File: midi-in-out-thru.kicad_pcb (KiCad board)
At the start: 2 copper layers, 72.6 x 48 mm, 19 parts, among them J1 uC, J2 IN, J3 OUT, J4 THRU, U1 74HC14, U2 H11L1

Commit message: Completed initial layout
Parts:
- added C3: 100n, Capacitor_THT:C_Disc_D3.8mm_W2.6mm_P2.50mm, F.Cu at (93.7, 52.1)
- added H1: MountingHole, MountingHole:MountingHole_3.2mm_M3, F.Cu at (86.0, 34.0)
- added H2: MountingHole, MountingHole:MountingHole_3.2mm_M3, F.Cu at (154.0, 34.0)
- added H3: MountingHole, MountingHole:MountingHole_3.2mm_M3, F.Cu at (86.0, 66.0)
- added H4: MountingHole, MountingHole:MountingHole_3.2mm_M3, F.Cu at (154.0, 66.0)
- J2, J3, J4: footprint eurocad:MIDI_DIN5 -> Personal:MIDI_DIN5
- moved J1 27.5 mm to (150.0, 52.8), turned to 0 degrees
- moved D1 16.3 mm to (87.6, 59.2), turned to 90 degrees
- moved C1 11.4 mm to (107.4, 52.1), turned to 0 degrees
- moved R8 10.9 mm to (140.2, 52.1), turned to 180 degrees
- moved R1 10.7 mm to (140.2, 63.0), turned to 180 degrees
- moved R3 9.88 mm to (103.9, 53.3), turned to -90 degrees
- moved R6 8.87 mm to (123.7, 52.1), turned to 180 degrees
- moved U1 6.48 mm to (108.0, 63.0)
- moved U2 6.23 mm to (94.7, 63.0)
- moved R7 5.95 mm to (127.3, 63.0), turned to 90 degrees
- moved R5 5.43 mm to (90.7, 61.7)
- moved R2 5.11 mm to (140.2, 55.6)
- moved LED1 3.74 mm to (143.8, 59.3), turned to -90 degrees
- moved LED2 3.21 mm to (143.8, 52.6)
- moved C2 2.05 mm to (98.6, 52.1)
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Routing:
- net /RX: track 0.00 -> 62.7 mm
- net /TX: track 0.00 -> 48.2 mm
- net Net-(D1-Pad2): track 0.00 -> 36.7 mm
- net Net-(J4-Pad5): track 0.00 -> 21.2 mm
- net Net-(R1-Pad2): track 0.00 -> 21.1 mm
- net Net-(R2-Pad2): track 0.00 -> 18.6 mm
- net Net-(C2-Pad1): track 0.00 -> 10.3 mm
- net Net-(J4-Pad4): track 0.00 -> 9.25 mm
- net Net-(J3-Pad5): track 0.00 -> 8.90 mm
- net Net-(D1-Pad1): track 0.00 -> 8.69 mm
- net Net-(R9-Pad1): track 0.00 -> 8.49 mm
- net Net-(J2-Pad4): track 0.00 -> 8.48 mm
- net Net-(J3-Pad4): track 0.00 -> 7.81 mm
- net Net-(R7-Pad1): track 0.00 -> 7.75 mm
- net Net-(LED1-Pad2): track 0.00 -> 4.08 mm
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- added copper zone on F.Cu, net +3.3V
- added copper zone on B.Cu, net GND
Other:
- board size 72.6 x 48 mm -> 76 x 40 mm
- copper layers 2 -> 4
- board text added: "GND"
- board text added: "IN"
- board text added: "MIDI In/Out/Thru Rev. 1"
- board text added: "OUT"
- board text added: "Paul Battley po-ru.com"
- board text added: "RX"
- board text added: "THRU"
- board text added: "TX"
- board text added: "VCC"
- board text added: "☐ 3.3V ☐ 5V"

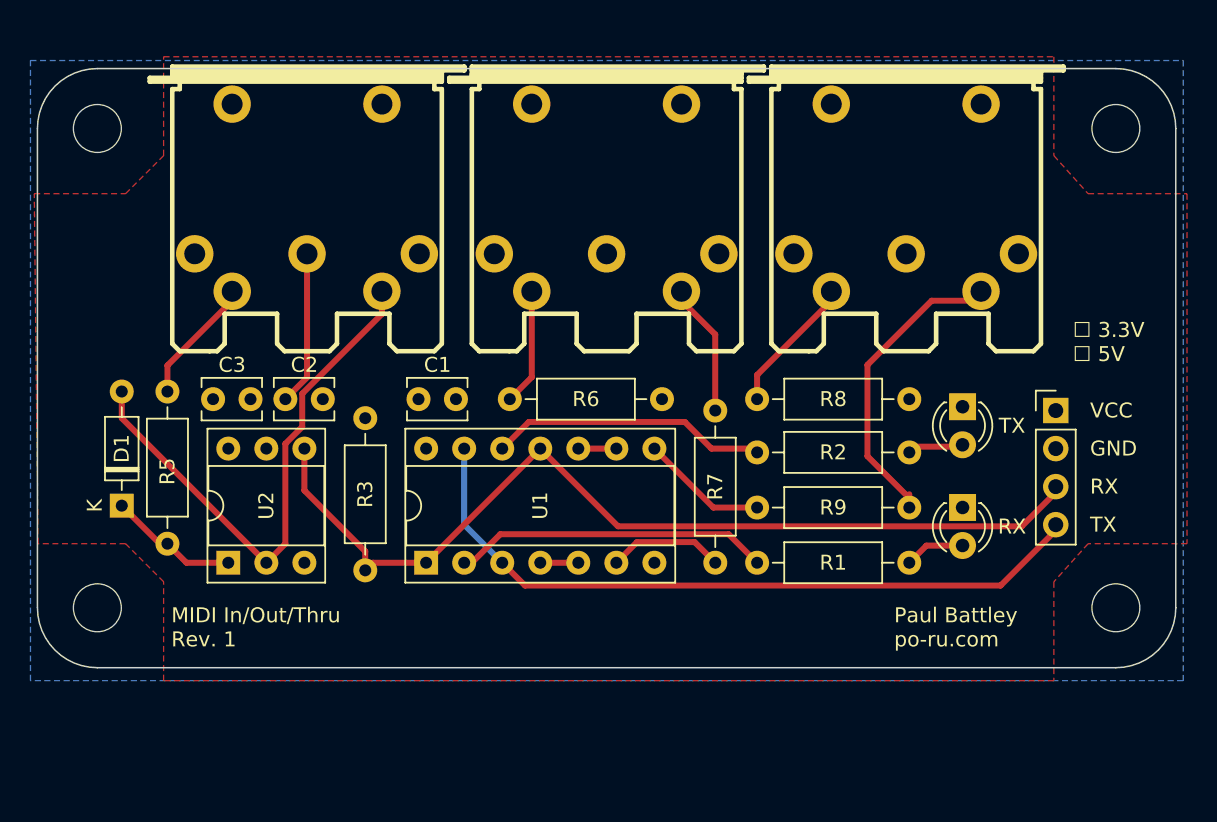
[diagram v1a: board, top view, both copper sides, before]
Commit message: Smaller resistors, neater layout
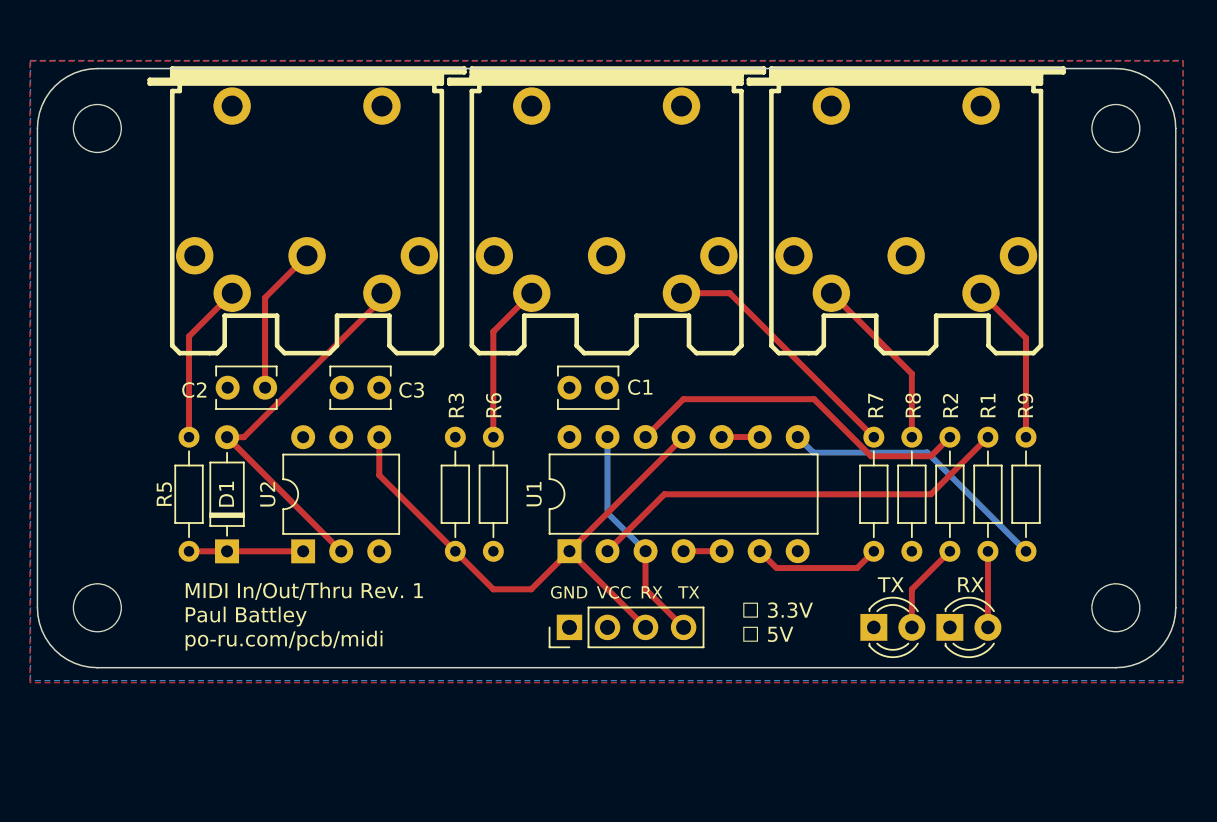
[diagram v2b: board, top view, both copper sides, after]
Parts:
- H1, H2, H3, H4: footprint MountingHole:MountingHole_3.2mm_M3 -> Personal:MountingHole_3.2mm_M3
- R1, R2, R3, R5, R6, R7, R8, R9: footprint Resistor_THT:R_Axial_DIN0207_L6.3mm_D2.5mm_P10.16mm_Horizontal -> Resistor_THT:R_Axial_DIN0204_L3.6mm_D1.6mm_P7.62mm_Horizontal
- U1: footprint Package_DIP:DIP-14_W7.62mm_Socket -> Package_DIP:DIP-14_W7.62mm
- U2: footprint Package_DIP:DIP-6_W7.62mm_Socket -> Package_DIP:DIP-6_W7.62mm
- moved J1 35.5 mm to (117.5, 67.3), turned to 90 degrees
- moved R9 18.2 mm to (148.0, 62.2), turned to 90 degrees
- moved LED2 15.9 mm to (137.8, 67.3), turned to 0 degrees
- moved R6 15.2 mm to (112.4, 62.2), turned to 90 degrees
- moved C3 11.1 mm to (104.8, 51.3), turned to 180 degrees
- moved R7 10.6 mm to (137.8, 62.2)
- moved R8 10.2 mm to (140.4, 62.2), turned to 90 degrees
- moved C1 10.1 mm to (117.5, 51.3)
- moved U1 9.60 mm to (117.5, 62.2)
- moved LED1 8.05 mm to (142.9, 67.3), turned to 0 degrees
- moved D1 7.66 mm to (94.7, 62.2)
- moved R2 7.14 mm to (142.9, 62.2), turned to 90 degrees
- moved R3 6.15 mm to (109.9, 54.6)
- moved R1 5.31 mm to (145.5, 62.2), turned to 90 degrees
- moved U2 5.06 mm to (99.7, 62.2)
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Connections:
- C3 pad 1: +3.3V -> GND
- J1 pad 1: +3.3V -> GND
- J1 pad 2: GND -> +3.3V
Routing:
- net /TX: track 48.2 -> 14.8 mm
- net /RX: track 62.7 -> 37.4 mm
- net Net-(D1-Pad2): track 36.7 -> 25.3 mm
- net Net-(J4-Pad5): track 21.2 -> 10.9 mm
- net Net-(R9-Pad1): track 8.49 -> 18.4 mm
- net Net-(J3-Pad5): track 8.90 -> 16.8 mm
- net Net-(R1-Pad2): track 21.1 -> 28.6 mm
- net Net-(R2-Pad2): track 18.6 -> 23.5 mm
- net Net-(J3-Pad4): track 7.81 -> 10.7 mm
- net Net-(J4-Pad4): track 9.25 -> 11.8 mm
- net Net-(LED2-Pad2): track 3.77 -> 6.13 mm
- net Net-(J2-Pad4): track 8.48 -> 10.8 mm
- net Net-(D1-Pad1): track 8.69 -> 7.62 mm
- net Net-(LED1-Pad2): track 4.08 -> 5.08 mm
- net Net-(R7-Pad1): track 7.75 -> 8.55 mm
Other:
- board text added: "MIDI In/Out/Thru Rev. 1 Paul Battley po-ru.com/pcb/midi"
- board text removed: "MIDI In/Out/Thru Rev. 1"
- board text removed: "Paul Battley po-ru.com"

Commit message: Tweak tracks before rounding
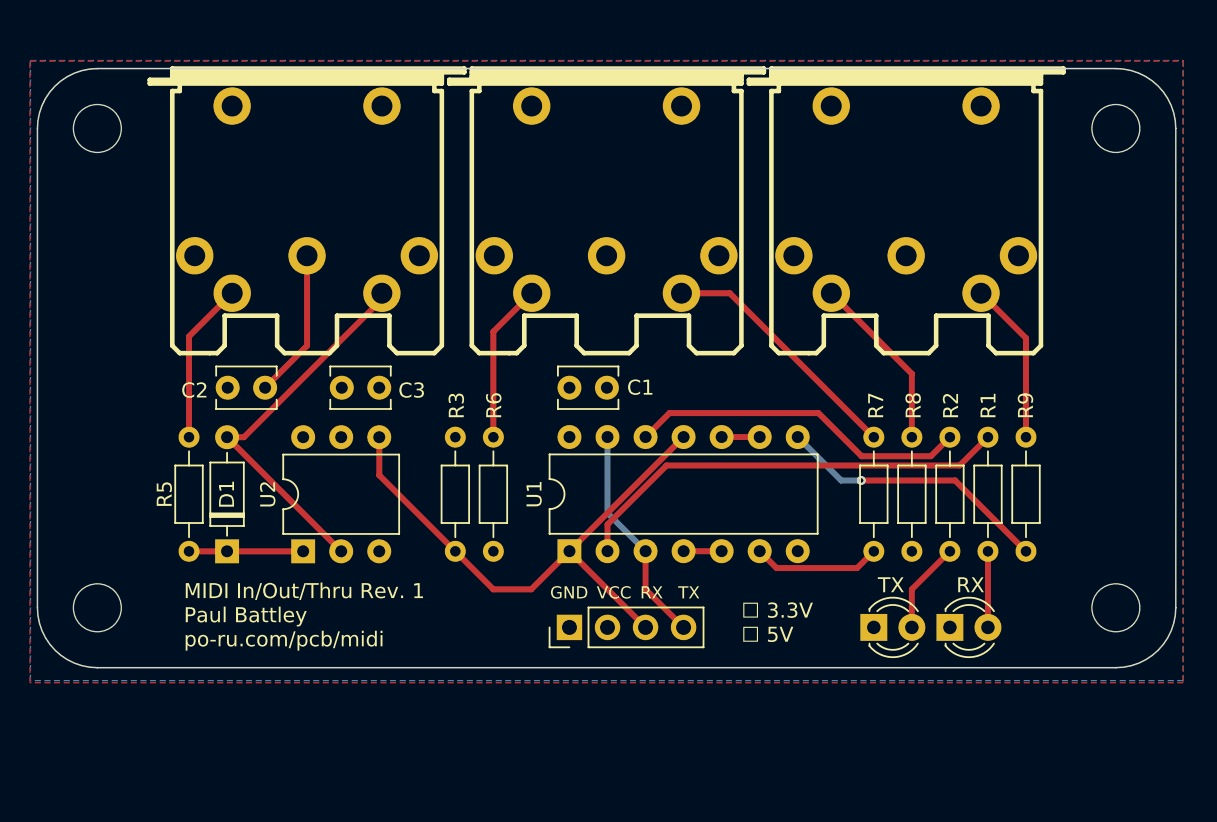
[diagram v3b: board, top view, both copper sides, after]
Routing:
- net Net-(R1-Pad2): track 28.6 -> 29.6 mm
- net Net-(R2-Pad2): track 23.5 -> 22.7 mm
- net Net-(R9-Pad1): vias 0 -> 1
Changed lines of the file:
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@@
     (effects (font (size 0.8128 0.8128) (thickness 0.1524)))
   )
-  (segment (start 97.2 45.29974) (end 97.2 51.308) (width 0.4) (layer "F.Cu") (net 3))
-  (segment (start 100 42.49974) (end 97.2 45.29974) (width 0.4) (layer "F.Cu") (net 3))
+  (segment (start 100 48.5) (end 97.2 51.3) (width 0.4) (layer "F.Cu") (net 3))
+  (segment (start 100 42.49974) (end 100 48.5) (width 0.4) (layer "F.Cu") (net 3))
+  (segment (start 97.2 51.3) (end 97.2 51.308) (width 0.4) (layer "F.Cu") (net 3))
   (segment (start 94.66 62.23) (end 99.74 62.23) (width 0.4) (layer "F.Cu") (net 4))
   (segment (start 92.12 62.23) (end 94.66 62.23) (width 0.4) (layer "F.Cu") (net 4))
@@
   (segment (start 148 48.00292) (end 148 54.61) (width 0.4) (layer "F.Cu") (net 9))
   (segment (start 144.99618 44.9991) (end 148 48.00292) (width 0.4) (layer "F.Cu") (net 9))
-  (segment (start 123.86 58.42) (end 141.65 58.42) (width 0.4) (layer "F.Cu") (net 10))
-  (segment (start 120.06 62.22) (end 123.86 58.42) (width 0.4) (layer "F.Cu") (net 10))
-  (segment (start 141.65 58.42) (end 145.46 54.61) (width 0.4) (layer "F.Cu") (net 10))
-  (segment (start 125.13 52.07) (end 133.847602 52.07) (width 0.4) (layer "F.Cu") (net 11))
+  (segment (start 120.06 60.44) (end 124 56.5) (width 0.4) (layer "F.Cu") (net 10))
+  (segment (start 120.06 62.22) (end 120.06 60.44) (width 0.4) (layer "F.Cu") (net 10))
+  (segment (start 143.57 56.5) (end 145.46 54.61) (width 0.4) (layer "F.Cu") (net 10))
+  (segment (start 124 56.5) (end 143.57 56.5) (width 0.4) (layer "F.Cu") (net 10))
+  (segment (start 124.2 53) (end 134.138801 53) (width 0.4) (layer "F.Cu") (net 11))
+  (segment (start 122.6 54.6) (end 124.2 53) (width 0.4) (layer "F.Cu") (net 11))
+  (segment (start 137.018801 55.88) (end 141.65 55.88) (width 0.4) (layer "F.Cu") (net 11))
+  (segment (start 134.138801 53) (end 137.018801 55.88) (width 0.4) (layer "F.Cu") (net 11))
   (segment (start 141.65 55.88) (end 142.92 54.61) (width 0.4) (layer "F.Cu") (net 11))
-  (segment (start 133.847602 52.07) (end 137.657602 55.88) (width 0.4) (layer "F.Cu") (net 11))
-  (segment (start 137.657602 55.88) (end 141.65 55.88) (width 0.4) (layer "F.Cu") (net 11))
-  (segment (start 122.6 54.6) (end 125.13 52.07) (width 0.4) (layer "F.Cu") (net 11))
   (segment (start 145.46 62.23) (end 145.46 67.31) (width 0.4) (layer "F.Cu") (net 12))
   (segment (start 115.00382 44.9991) (end 112.44 47.56292) (width 0.4) (layer "F.Cu") (net 13))
@@
   (segment (start 140.38 50.37528) (end 140.38 54.61) (width 0.4) (layer "F.Cu") (net 16))
   (segment (start 135.00382 44.9991) (end 140.38 50.37528) (width 0.4) (layer "F.Cu") (net 16))
-  (segment (start 132.76 54.6) (end 133.797 55.637) (width 0.4) (layer "B.Cu") (net 17))
-  (segment (start 141.407 55.637) (end 148 62.23) (width 0.4) (layer "B.Cu") (net 17))
-  (segment (start 133.797 55.637) (end 141.407 55.637) (width 0.4) (layer "B.Cu") (net 17))
+  (segment (start 143.27 57.5) (end 148 62.23) (width 0.4) (layer "F.Cu") (net 17))
+  (segment (start 137 57.5) (end 143.27 57.5) (width 0.4) (layer "F.Cu") (net 17))
+  (via (at 137 57.5) (size 0.6) (drill 0.3) (layers "F.Cu" "B.Cu") (net 17))
+  (segment (start 137 57.5) (end 135.66 57.5) (width 0.4) (layer "B.Cu") (net 17))
+  (segment (start 135.66 57.5) (end 132.76 54.6) (width 0.4) (layer "B.Cu") (net 17))
   (segment (start 136.723 63.347) (end 137.84 62.23) (width 0.4) (layer "F.Cu") (net 18))
   (segment (start 130.22 62.22) (end 131.347 63.347) (width 0.4) (layer "F.Cu") (net 18))

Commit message: Remove extra layers
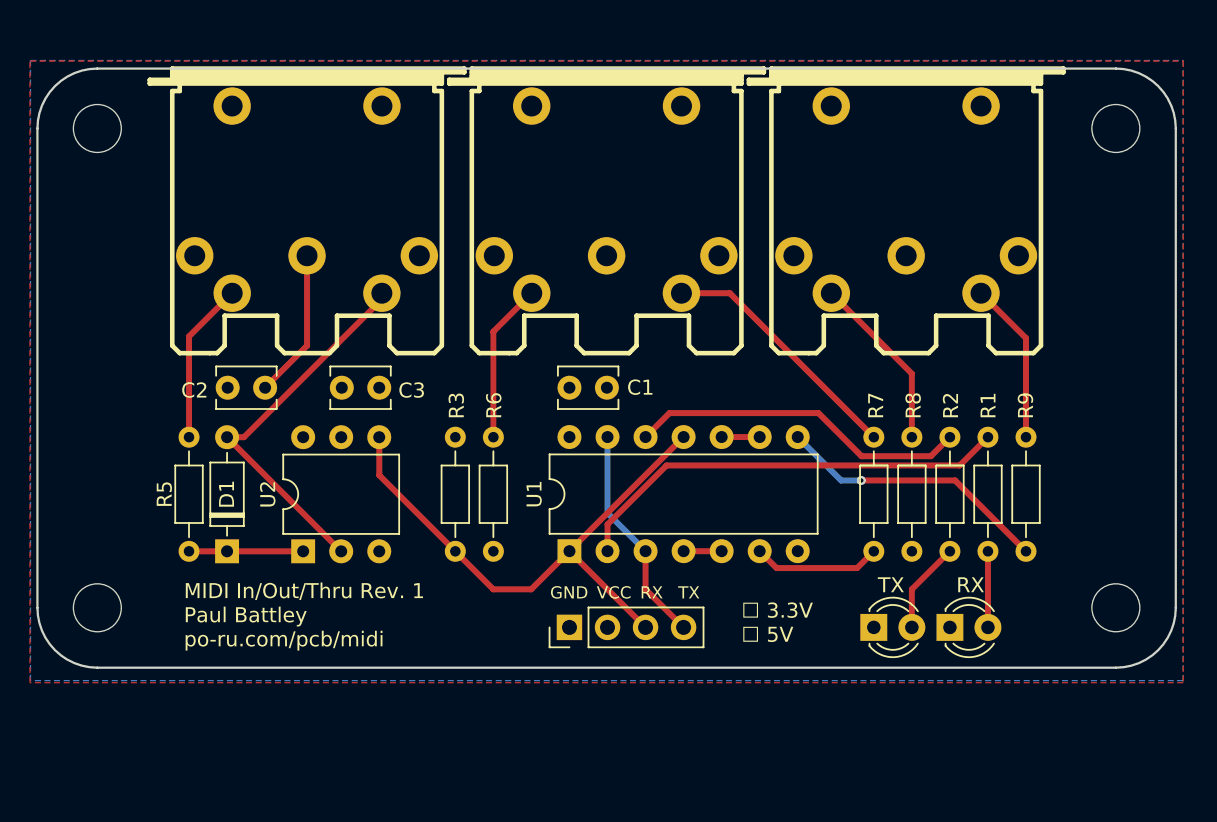
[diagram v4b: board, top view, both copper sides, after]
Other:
- copper layers 4 -> 2
- board text added: "JLCJLCJLCJLC"
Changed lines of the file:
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@@
 (kicad_pcb (version 20211014) (generator pcbnew)
   (general
-    (thickness 1.6)
+    (thickness 0.57)
   )
   (paper "A4")
   (layers
     (0 "F.Cu" signal "Front")
-    (1 "In1.Cu" signal)
-    (2 "In2.Cu" signal)
     (31 "B.Cu" signal "Back")
     (34 "B.Paste" user)
@@
       (layer "F.Cu" (type "copper") (thickness 0.035))
       (layer "dielectric 1" (type "core") (thickness 0.48) (material "FR4") (epsilon_r 4.5) (loss_tangent 0.02))
-      (layer "In1.Cu" (type "copper") (thickness 0.035))
-      (layer "dielectric 2" (type "prepreg") (thickness 0.48) (material "FR4") (epsilon_r 4.5) (loss_tangent 0.02))
-      (layer "In2.Cu" (type "copper") (thickness 0.035))
-      (layer "dielectric 3" (type "core") (thickness 0.48) (material "FR4") (epsilon_r 4.5) (loss_tangent 0.02))
       (layer "B.Cu" (type "copper") (thickness 0.035))
       (layer "B.Mask" (type "Bottom Solder Mask") (thickness 0.01))
@@
     )
   )
-  (gr_line (start 82 66) (end 82 34) (layer "Edge.Cuts") (width 0.1))
-  (gr_line (start 86 30) (end 154 30) (layer "Edge.Cuts") (width 0.1))
-  (gr_line (start 154 70) (end 86 70) (layer "Edge.Cuts") (width 0.1))
-  (gr_arc (start 158 66) (mid 156.828427 68.828427) (end 154 70) (layer "Edge.Cuts") (width 0.1))
-  (gr_arc (start 86 70) (mid 83.171573 68.828427) (end 82 66) (layer "Edge.Cuts") (width 0.1))
-  (gr_arc (start 82 34) (mid 83.171573 31.171573) (end 86 30) (layer "Edge.Cuts") (width 0.1))
-  (gr_arc (start 154 30) (mid 156.828427 31.171573) (end 158 34) (layer "Edge.Cuts") (width 0.1))
-  (gr_line (start 158 34) (end 158 66) (layer "Edge.Cuts") (width 0.1))
+  (gr_line (start 82 66) (end 82 34) (layer "Edge.Cuts") (width 0.15))
+  (gr_line (start 86 30) (end 154 30) (layer "Edge.Cuts") (width 0.15))
+  (gr_line (start 154 70) (end 86 70) (layer "Edge.Cuts") (width 0.15))
+  (gr_arc (start 158 66) (mid 156.828427 68.828427) (end 154 70) (layer "Edge.Cuts") (width 0.15))
+  (gr_arc (start 86 70) (mid 83.171573 68.828427) (end 82 66) (layer "Edge.Cuts") (width 0.15))
+  (gr_arc (start 82 34) (mid 83.171573 31.171573) (end 86 30) (layer "Edge.Cuts") (width 0.15))
+  (gr_arc (start 154 30) (mid 156.828427 31.171573) (end 158 34) (layer "Edge.Cuts") (width 0.15))
+  (gr_line (start 158 34) (end 158 66) (layer "Edge.Cuts") (width 0.15))
   (gr_text "IN" (at 99.822 37.592 90) (layer "B.SilkS")
     (effects (font (size 1.524 1.524) (thickness 0.3048)) (justify mirror))
@@
     (effects (font (size 1.524 1.524) (thickness 0.3048)) (justify mirror))
   )
+  (gr_text "JLCJLCJLCJLC" (at 102.5 66.5) (layer "B.SilkS")
+    (effects (font (size 0.8128 0.8128) (thickness 0.1524)) (justify mirror))
+  )
   (gr_text "GND" (at 117.5 65) (layer "F.SilkS")
